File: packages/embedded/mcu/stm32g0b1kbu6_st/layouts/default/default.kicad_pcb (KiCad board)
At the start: 2 copper layers, 5 parts

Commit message: Make package builds deterministic by wiring explicit local parts
The remaining packages now reference package-local concrete passives,
inductors, and other small parts directly instead of relying on generic
part-picker resolution. This aligns the source with the local
assets and removes the flaky live EasyEDA lookup path that was blocking
verification.

Constraint: Builds must not depend on unstable live part-picking when local package assets already exist
Constraint: Package-local parts remain the ownership boundary; no shared global part store was introduced
Rejected: Keep generic passives as the default style | repeated verification failures from upstream EasyEDA API instability
Rejected: Add ad hoc offline hacks around ato part-picking | weaker than making the package source deterministic
Confidence: high
Scope-risk: moderate
Reversibility: clean
Directive: For packages that already own generated local parts, instantiate those part modules directly and avoid generic passive declarations unless there is a strong reason not to
Tested:  passed for stm32g0b1kbu6_st, mcp2518fdt_e_sl_microchip, tcan3413ddfr_ti, raspberry_pi_hat_socket_zhouri, bq40z50rsmr_r2_4s_3a_ti, tps56637rpar_5v1_5a_ti, tps62933drlr_3v3_ti, bq25756rrvr_4s_2a_ti, tps2121ruxr_20v_4a_ti, and tps25730drefr_20v_3a_ti
Not-tested: Cross-package downstream integration beyond each package's default/example build
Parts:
- C1, C3: value 100nF ±10% -> (none)
- C2: value 4.7µF ±10% -> (none)
- R1: value 10kΩ ±1% -> (none)
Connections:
- C1 pad 1: hv -> PF2_NRST
- C2 pad 1: supply_bypass-power-hv -> hv
- C3 pad 1: supply_bypass-power-hv -> hv
- U1 pad 4: supply_bypass-power-hv -> hv
- U1 pad 6: hv -> PF2_NRST
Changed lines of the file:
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@@
 	(net 26 "PB7")
 	(net 27 "PB8")
-	(net 28 "hv")
+	(net 28 "PF2_NRST")
 	(net 29 "PA0")
 	(net 30 "PA1")
 	(net 31 "PA2")
-	(net 32 "supply_bypass-power-hv")
+	(net 32 "hv")
 	(footprint "STMicroelectronics_STM32G0B1KBU6:QFN-32_L5.0-W5.0-P0.50-TL-EP3.5"
 		(layer "F.Cu")
@@
 			(size 0.8 0.28)
 			(layers "F.Cu" "F.Paste" "F.Mask")
-			(net 32 "supply_bypass-power-hv")
+			(net 32 "hv")
 		)
 		(pad "5" smd oval
@@
 			(size 0.8 0.28)
 			(layers "F.Cu" "F.Paste" "F.Mask")
-			(net 28 "hv")
+			(net 28 "PF2_NRST")
 		)
 		(pad "7" smd oval
@@
 			)
 		)
-		(property "Value" "10kΩ ±1%"
+		(property "Value" ""
 			(at 0 4)
 			(layer "F.Fab")
@@
 			(hide yes)
 		)
-		(property "Datasheet" "https://www.lcsc.com/datasheet/lcsc_datasheet_1811141608_YAGEO-RC0402FR-0710KL_C60490.pdf"
+		(property "Datasheet" "https://www.lcsc.com/datasheet/lcsc_datasheet_2304140030_YAGEO-RC0402FR-0710KL_C60490.pdf"
 			(at 0 0 0)
 			(layer "User.9")
@@
 			)
 		)
-		(property "Value" "100nF ±10%"
+		(property "Value" ""
 			(at 0 4)
 			(layer "F.Fab")
@@
 			(size 0.5 0.54)
 			(layers "F.Cu" "F.Paste" "F.Mask")
-			(net 28 "hv")
+			(net 28 "PF2_NRST")
 		)
 		(embedded_fonts no)
@@
 			)
 		)
-		(property "Value" "100nF ±10%"
+		(property "Value" ""
 			(at 0 4)
 			(layer "F.Fab")
@@
 			(size 0.5 0.54)
 			(layers "F.Cu" "F.Paste" "F.Mask")
-			(net 32 "supply_bypass-power-hv")
+			(net 32 "hv")
 		)
 		(embedded_fonts no)
@@
 			)
 		)
-		(property "Value" "4.7µF ±10%"
+		(property "Value" ""
 			(at 0 4)
 			(layer "F.Fab")
@@
 			(size 0.8 0.9)
 			(layers "F.Cu" "F.Paste" "F.Mask")
-			(net 32 "supply_bypass-power-hv")
+			(net 32 "hv")
 		)
 		(embedded_fonts no)

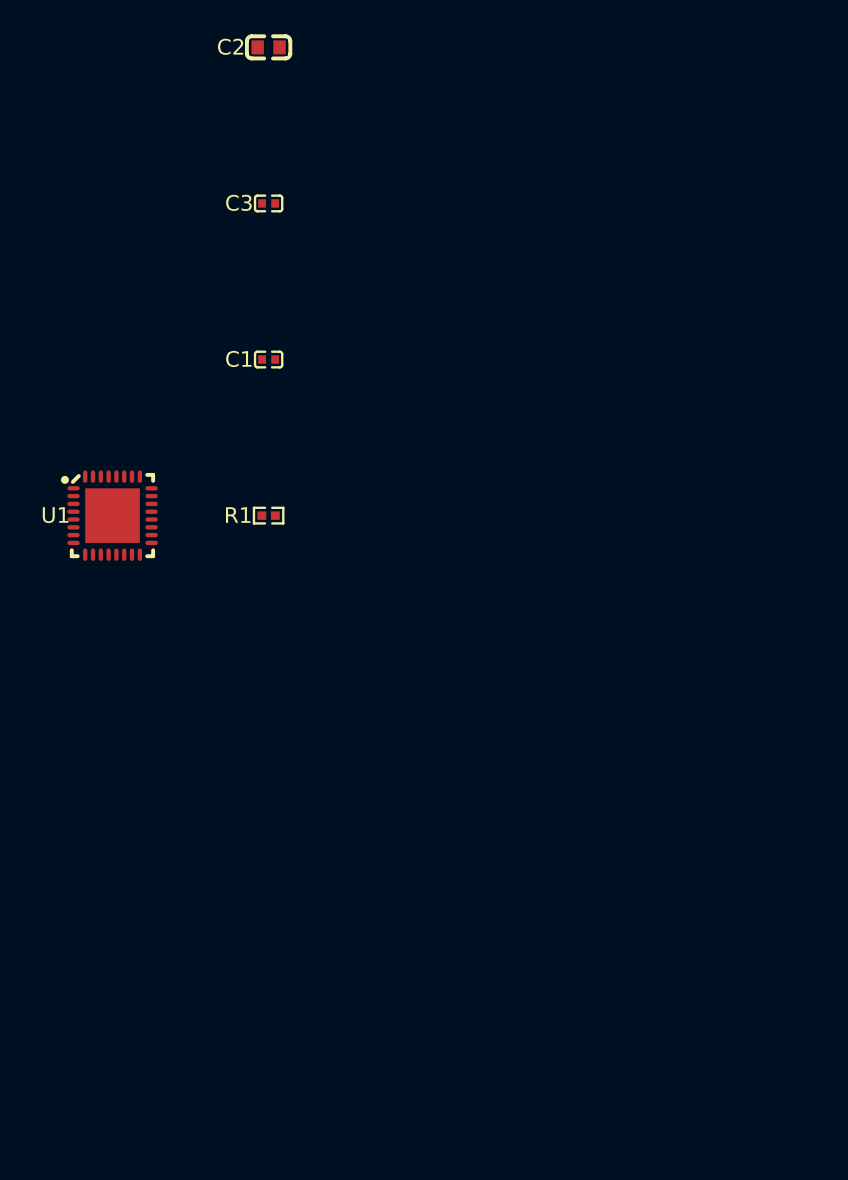
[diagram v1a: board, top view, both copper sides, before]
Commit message: STM32G0 update
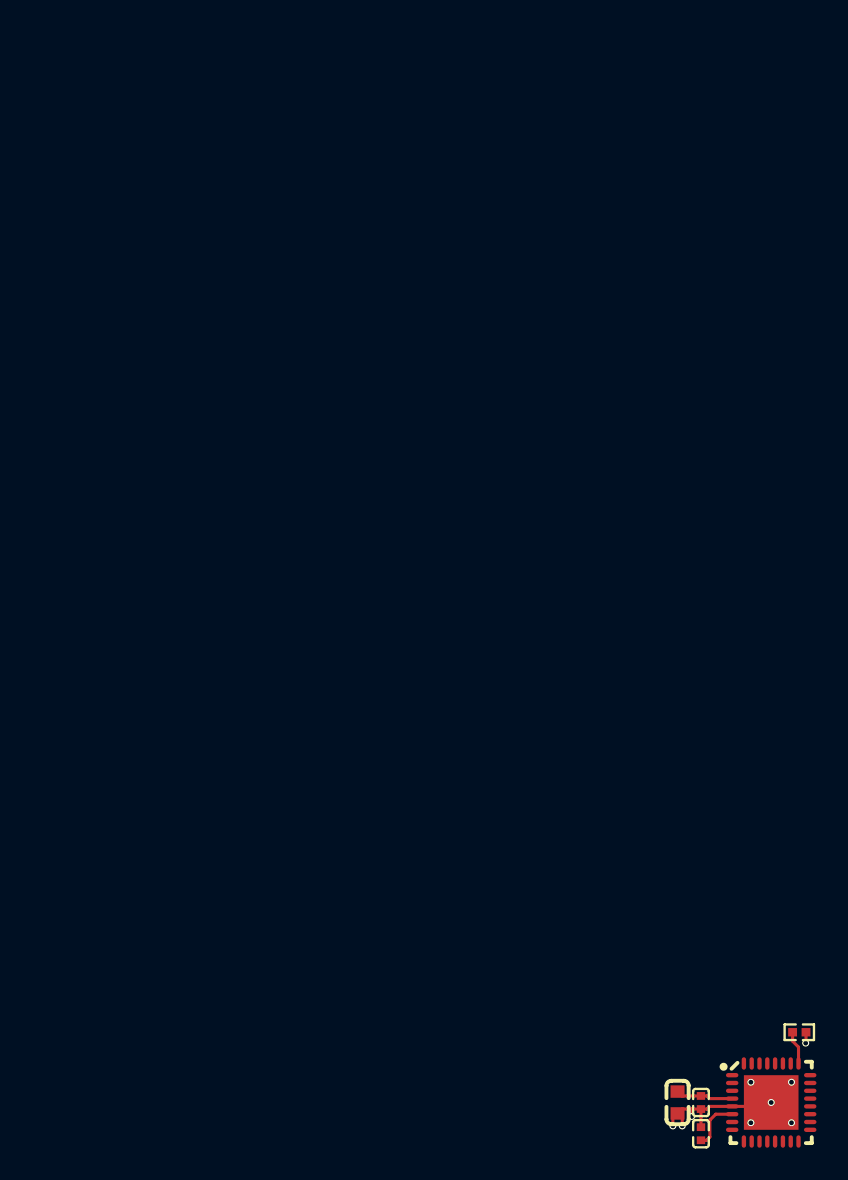
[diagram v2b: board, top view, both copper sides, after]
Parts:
- moved C2 72.5 mm to (36.2, 37.6), turned to -90 degrees
- moved C3 63.9 mm to (37.7, 37.6), turned to -90 degrees
- moved C1 56.8 mm to (37.7, 39.6), turned to 90 degrees
- moved U1 56.5 mm to (42.2, 37.6)
- moved R1 47.5 mm to (44.0, 33.1)
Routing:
- net lv: track 0.00 -> 10.5 mm, vias 0 -> 9
- net hv: track 0.00 -> 3.69 mm
- net PF2_NRST: track 0.00 -> 3.32 mm
- net PA14_BOOT0: track 0.00 -> 2.16 mm
